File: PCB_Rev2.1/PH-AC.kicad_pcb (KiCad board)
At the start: 2 copper layers, 200 x 100 mm, 68 parts, among them J1 USB_C_Receptacle_USB2.0_14P, J2 Conn_01x03, Q1 DMG1012T, SW1 SW_Push, SW10 SW_Push, SW2 RotaryEncoder_Switch_MP, SW3 RotaryEncoder_Switch_MP, SW4 SW_Push, SW5 SW_Push, SW6 SW_Push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

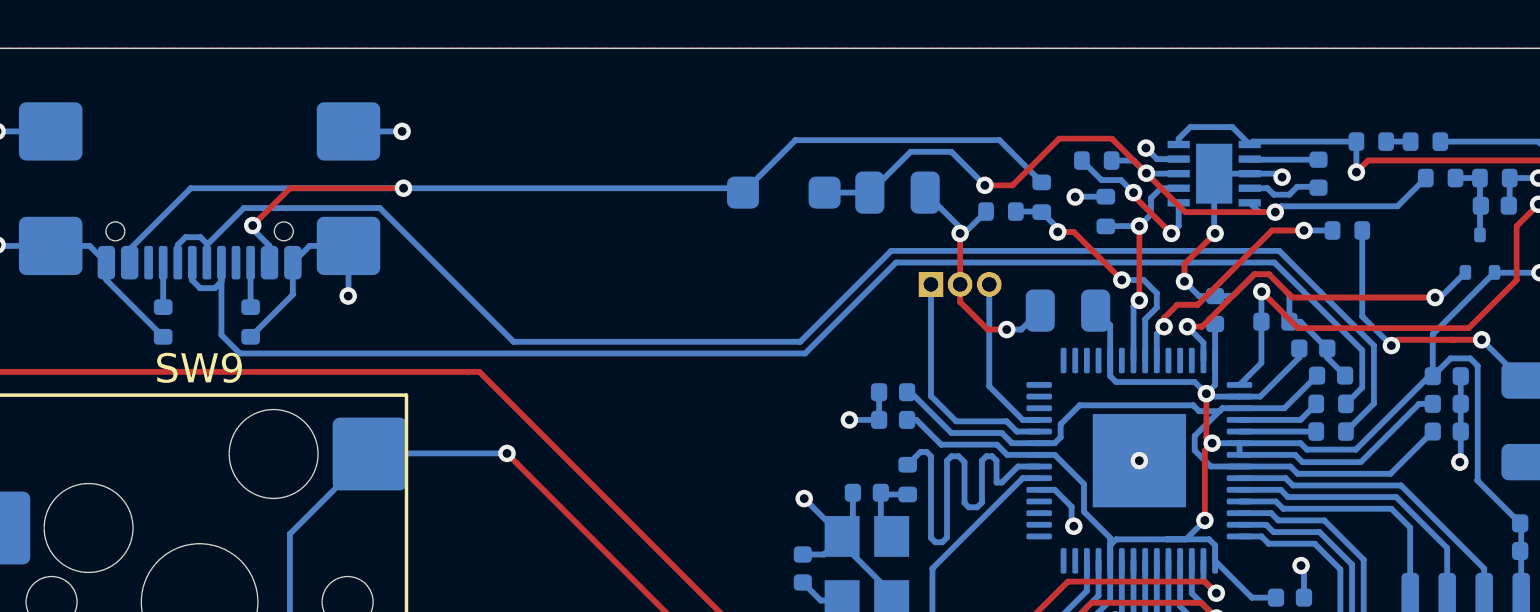
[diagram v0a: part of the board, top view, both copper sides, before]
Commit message: Minor Update
Fixed wiring mistake of D+ and D-.
Decreased the thickness of upper panel to 1.4mm
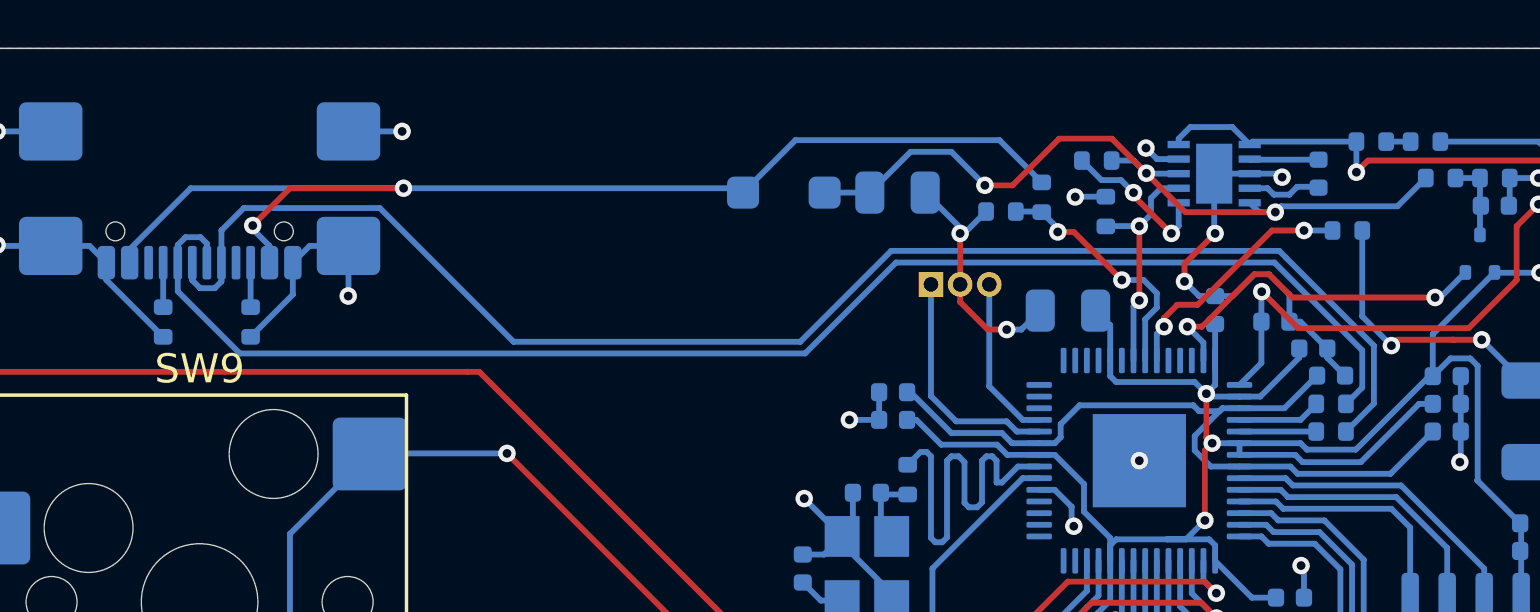
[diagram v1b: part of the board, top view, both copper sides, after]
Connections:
- R3 pad 1: /USB_DM -> /USB_DP
- R4 pad 1: /USB_DP -> /USB_DM
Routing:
- net /USB_DP: track 49.0 -> 51.3 mm
- net /USB_DM: track 51.5 -> 50.2 mm
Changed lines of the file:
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@@
 			(layers "B.Cu" "B.Paste" "B.Mask")
 			(roundrect_rratio 0.25)
-			(net 19 "/USB_DM")
+			(net 18 "/USB_DP")
 			(pintype "passive")
 		)
@@
 			(layers "B.Cu" "B.Paste" "B.Mask")
 			(roundrect_rratio 0.25)
-			(net 18 "/USB_DP")
+			(net 19 "/USB_DM")
 			(pintype "passive")
 		)
@@
 	)
 	(segment
-		(start 206.84 65.2)
-		(end 207.4 64.64)
+		(start 207.8 65.19)
+		(end 207.8 63.198629)
 		(width 0.2)
 		(layer "B.Cu")
@@
 	)
 	(segment
-		(start 168.881076 63.47)
-		(end 168.25 62.838924)
+		(start 188.114314 63.07)
+		(end 178.274744 63.07)
 		(width 0.2)
 		(layer "B.Cu")
@@
 	)
 	(segment
-		(start 207.4 63.364315)
-		(end 204.385685 60.35)
+		(start 206.84 66.15)
+		(end 207.8 65.19)
 		(width 0.2)
 		(layer "B.Cu")
@@
 	)
 	(segment
-		(start 168.25 62.838924)
-		(end 168.25 60.355)
+		(start 207.8 63.198629)
+		(end 204.785685 60.184315)
 		(width 0.2)
 		(layer "B.Cu")
@@
 	)
 	(segment
-		(start 191.4 60.35)
-		(end 188.28 63.47)
+		(start 178.274744 63.07)
+		(end 173.684744 58.48)
 		(width 0.2)
 		(layer "B.Cu")
@@
 	)
 	(segment
+		(start 191.234314 59.95)
+		(end 188.114314 63.07)
+		(width 0.2)
+		(layer "B.Cu")
+		(net 18)
+	)
+	(segment
+		(start 168.25 59.24759)
+		(end 168.25 60.355)
+		(width 0.2)
+		(layer "B.Cu")
+		(net 18)
+	)
+	(segment
 		(start 167.25 60.355)
 		(end 167.25 60.96241)
@@
 	)
 	(segment
+		(start 204.785685 60.184315)
+		(end 204.551371 59.95)
+		(width 0.2)
+		(layer "B.Cu")
+		(net 18)
+	)
+	(segment
 		(start 168.25 61)
 		(end 168.25 60.355)
@@
 	)
 	(segment
-		(start 207.4 64.64)
-		(end 207.4 63.364315)
+		(start 169.01759 58.48)
+		(end 168.25 59.24759)
 		(width 0.2)
 		(layer "B.Cu")
@@
 	)
 	(segment
-		(start 188.28 63.47)
-		(end 168.881076 63.47)
+		(start 173.684744 58.48)
+		(end 169.01759 58.48)
 		(width 0.2)
 		(layer "B.Cu")
@@
 	)
 	(segment
-		(start 204.385685 60.35)
-		(end 191.4 60.35)
+		(start 204.551371 59.95)
+		(end 191.234314 59.95)
 		(width 0.2)
 		(layer "B.Cu")
@@
 	)
 	(segment
-		(start 207.8 65.19)
-		(end 207.8 63.198629)
+		(start 166.75 59.74759)
+		(end 167.01759 59.48)
 		(width 0.2)
 		(layer "B.Cu")
@@
 	)
 	(segment
-		(start 166.75 59.74759)
-		(end 167.01759 59.48)
+		(start 166.75 61.338924)
+		(end 168.881076 63.47)
 		(width 0.2)
 		(layer "B.Cu")
@@
 	)
 	(segment
-		(start 188.114314 63.07)
-		(end 178.274744 63.07)
+		(start 166.75 60.355)
+		(end 166.75 59.74759)
 		(width 0.2)
 		(layer "B.Cu")
@@
 	)
 	(segment
-		(start 206.84 66.15)
-		(end 207.8 65.19)
+		(start 168.881076 63.47)
+		(end 188.28 63.47)
 		(width 0.2)
 		(layer "B.Cu")
@@
 	)
 	(segment
-		(start 207.8 63.198629)
-		(end 204.785685 60.184315)
+		(start 188.28 63.47)
+		(end 191.4 60.35)
 		(width 0.2)
 		(layer "B.Cu")
@@
 	)
 	(segment
-		(start 166.75 60.355)
-		(end 166.75 59.74759)
+		(start 191.4 60.35)
+		(end 204.385685 60.35)
 		(width 0.2)
 		(layer "B.Cu")
@@
 	)
 	(segment
-		(start 178.274744 63.07)
-		(end 173.684744 58.48)
+		(start 166.75 60.355)
+		(end 166.75 61.338924)
 		(width 0.2)
 		(layer "B.Cu")
@@
 	)
 	(segment
-		(start 191.234314 59.95)
-		(end 188.114314 63.07)
+		(start 207.4 64.64)
+		(end 206.84 65.2)
 		(width 0.2)
 		(layer "B.Cu")
@@
 	)
 	(segment
-		(start 167.75 59.7)
-		(end 167.75 60.355)
+		(start 207.4 63.364315)
+		(end 207.4 64.64)
 		(width 0.2)
 		(layer "B.Cu")
@@
 	)
 	(segment
-		(start 169.01759 58.48)
-		(end 167.75 59.74759)
+		(start 204.385685 60.35)
+		(end 207.4 63.364315)
 		(width 0.2)
 		(layer "B.Cu")
@@
 	)
 	(segment
-		(start 204.785685 60.184315)
-		(end 204.551371 59.95)
+		(start 167.75 59.7)
+		(end 167.75 60.355)
 		(width 0.2)
 		(layer "B.Cu")
@@
 	)
 	(segment
-		(start 173.684744 58.48)
-		(end 169.01759 58.48)
-		(width 0.2)
-		(layer "B.Cu")
-		(net 19)
-	)
-	(segment
 		(start 167.53 59.48)
 		(end 167.75 59.7)
 		(width 0.2)
 		(layer "B.Cu")
-		(net 19)
-	)
-	(segment
-		(start 204.551371 59.95)
-		(end 191.234314 59.95)
-		(width 0.2)
-		(layer "B.Cu")

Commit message: Detail Improvement
Changed the package size of diodes from 0402 to 0805.
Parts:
- D3, D4, D5, D6, D7, D8, D9: footprint Diode_SMD:D_0402_1005Metric -> Diode_SMD:D_0805_2012Metric
- SW10, SW8: footprint PCM_Switch_Keyboard_Hotswap_Kailh:SW_Hotswap_Kailh_MX_2.75u -> PCM_Switch_Keyboard_Hotswap_Kailh:SW_Hotswap_Kailh_MX_2.25u
- moved D3 2.00 mm to (111.0, 100.0)
- moved D4 2.00 mm to (144.0, 100.0)
- moved D5 2.00 mm to (177.0, 100.0)
- moved D6 2.00 mm to (210.0, 100.0)
- moved D7 2.00 mm to (127.5, 142.0)
- moved D8 2.00 mm to (160.5, 76.0)
- moved D9 2.00 mm to (193.5, 142.0)
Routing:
- net ROW1: track 228.0 -> 223.5 mm
- net Net-(D9-A): track 4.09 -> 5.64 mm
- net Net-(D7-A): track 4.09 -> 5.64 mm
- net Net-(D8-A): track 4.09 -> 5.64 mm
- net Net-(D6-A): track 4.09 -> 5.64 mm
- net Net-(D5-A): track 4.09 -> 5.64 mm
- net Net-(D4-A): track 4.09 -> 5.64 mm
- net Net-(D3-A): track 4.09 -> 5.64 mm
- net ROW0: track 134.4 -> 133.4 mm

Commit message: Case Improvement
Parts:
- D1: value D_Schottky -> MBR120VLSFT1G
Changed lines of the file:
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@@
 			)
 		)
-		(property "Value" "D_Schottky"
+		(property "Value" "MBR120VLSFT1G"
 			(at 0 -2.1 0)
 			(layer "B.Fab")

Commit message: Design Modification
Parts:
- removed D3, D4, D5, D6, D7, D8, D9: D, Diode_SMD:D_0805_2012Metric
- moved C8 1.92 mm to (193.1, 65.4)
- moved C3 1.92 mm to (193.1, 66.3)
- moved R12 1.68 mm to (190.3, 68.7)
- moved Y1 1.68 mm to (188.9, 71.7)
- moved C18 1.68 mm to (188.9, 69.1)
- moved C17 1.68 mm to (186.8, 71.7)
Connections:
- SW10 pad 1: Net-(D9-A) -> BT6
- SW10 pad 2: COL2 -> GND
- SW2 pad A: ENC1A -> ENC2A
- SW2 pad B: ENC1B -> ENC2B
- SW3 pad A: ENC2A -> ENC1A
- SW3 pad B: ENC2B -> ENC1B
- SW4 pad 1: Net-(D3-A) -> BT0
- SW4 pad 2: COL0 -> GND
- SW5 pad 1: Net-(D4-A) -> BT1
- SW5 pad 2: COL1 -> GND
- SW6 pad 1: Net-(D5-A) -> BT2
- SW6 pad 2: COL2 -> GND
- SW7 pad 1: Net-(D6-A) -> BT3
- SW7 pad 2: COL3 -> GND
- SW8 pad 1: Net-(D7-A) -> BT4
- SW8 pad 2: COL0 -> GND
- SW9 pad 1: Net-(D8-A) -> BT5
- SW9 pad 2: COL1 -> GND
- U1 pad 11: ENC2A -> ENC1B
- U1 pad 13: unconnected-(U1-GPIO10-Pad13) -> ENC2A
- U1 pad 2: COL0 -> BT6
- U1 pad 3: COL1 -> BT5
- U1 pad 4: COL2 -> BT4
- U1 pad 5: COL3 -> BT3
- U1 pad 6: ROW0 -> BT2
- U1 pad 7: ROW1 -> BT1
- U1 pad 8: ENC1A -> BT0
- U1 pad 9: ENC1B -> ENC1A
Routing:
- net ROW1: track 223.5 -> 0.00 mm, vias 3 -> 0
- net COL0: track 156.3 -> 0.00 mm, vias 2 -> 0
- net ROW0: track 133.4 -> 0.00 mm, vias 5 -> 0
- net BT4: track 0.00 -> 125.5 mm, vias 0 -> 2
- net BT0: track 0.00 -> 105.3 mm, vias 0 -> 2
- net ENC1A: track 150.2 -> 64.1 mm, vias 1 -> 0
- net COL2: track 76.0 -> 0.00 mm, vias 2 -> 0
- net BT1: track 0.00 -> 74.1 mm, vias 0 -> 2
- net ENC2A: track 64.3 -> 134.8 mm
- net BT6: track 0.00 -> 70.0 mm, vias 0 -> 2
- net COL1: track 67.1 -> 0.00 mm, vias 2 -> 0
- net ENC1B: track 128.6 -> 64.1 mm, vias 1 -> 0
- net ENC2B: track 63.0 -> 126.9 mm
- net BT5: track 0.00 -> 59.5 mm, vias 0 -> 2
- net GND: track 74.0 -> 120.1 mm, vias 23 -> 31
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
